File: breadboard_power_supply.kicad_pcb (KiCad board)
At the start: 2 copper layers, 50.8 x 27.8 mm, 27 parts, among them J1 Conn_02x02_Odd_Even, J2 Conn_02x02_Odd_Even, J3 Conn_02x03_Odd_Even, J4 Conn_02x03_Odd_Even, J5 7010ASV, U1 CH224K, U2 AP63205, U3 AP2205-33Y

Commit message: part placement done, started routing of top layer
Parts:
- removed C4: 10u, 0Capacitors:C_0805_2012Metric_Pad1.18x1.45mm_HandSolder
- moved R4 149.1 mm to (182.0, 78.6), turned to -90 degrees
- moved R5 145.4 mm to (178.6, 78.6), turned to -90 degrees
- moved R6 141.8 mm to (175.2, 78.6), turned to -90 degrees
- moved JP1 140.2 mm to (182.0, 74.0), turned to -90 degrees
- moved JP2 136.4 mm to (178.6, 74.0), turned to -90 degrees
- moved R3 135.5 mm to (166.6, 86.0)
- moved C8 135.0 mm to (164.2, 77.6), turned to 90 degrees
- moved U1 134.0 mm to (160.0, 86.0), turned to -90 degrees
- moved JP3 132.7 mm to (175.2, 74.0), turned to -90 degrees
- moved R1 129.5 mm to (159.2, 76.6), turned to -90 degrees
- moved C9 129.3 mm to (158.2, 82.4)
- moved C3 128.9 mm to (157.6, 76.0), turned to 90 degrees
- moved R2 127.5 mm to (159.2, 79.8), turned to -90 degrees
- moved C1 126.3 mm to (154.0, 79.2)
- moved C7 124.5 mm to (162.2, 77.6), turned to 90 degrees
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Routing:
- net /CFG2: track 0.00 -> 38.6 mm, vias 0 -> 2
- net /CFG3: track 0.00 -> 34.4 mm, vias 0 -> 2
- net /CC1: track 0.00 -> 34.2 mm, vias 0 -> 2
- net /CC2: track 0.00 -> 32.3 mm
- net /CFG1: track 0.00 -> 28.2 mm
- net /USB_P: track 0.00 -> 27.1 mm
- net /USB_N: track 0.00 -> 27.1 mm, vias 0 -> 2
- net VBUS: track 0.00 -> 19.9 mm, vias 0 -> 1
- net Net-(U1-Vdd): track 0.00 -> 4.85 mm
- net Net-(U1-VBUS): track 0.00 -> 3.18 mm
- net GND: track 0.00 -> 2.74 mm
- net Net-(U2-SW): track 0.00 -> 2.11 mm
- net Net-(R1-Pad2): track 0.00 -> 1.53 mm

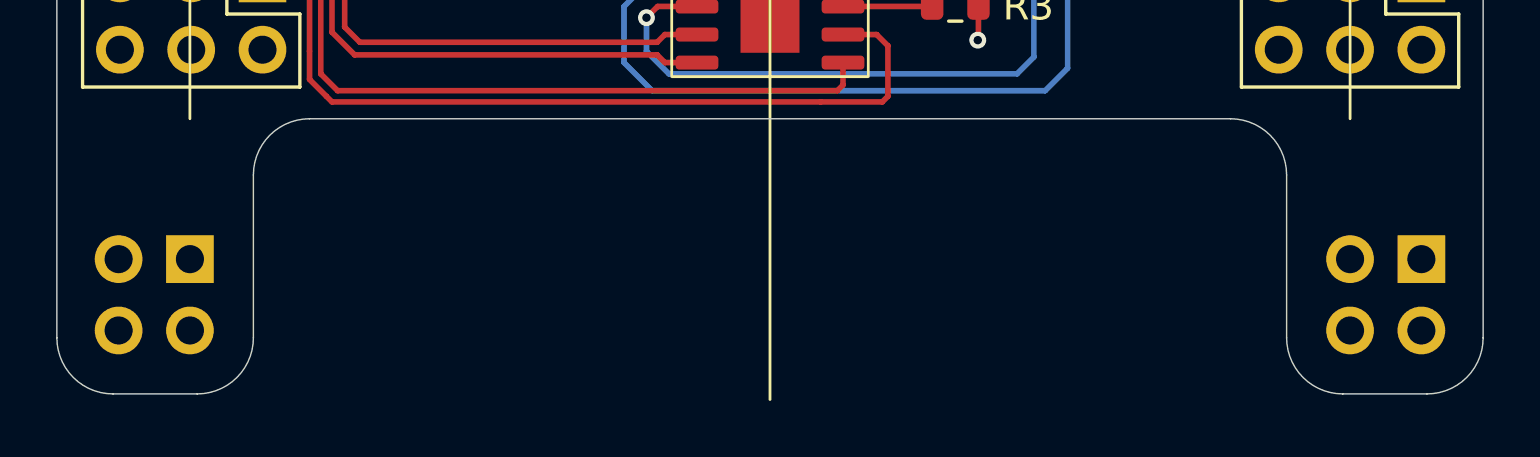
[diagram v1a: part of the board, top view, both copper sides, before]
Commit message: adjusted position for breadboard connectors
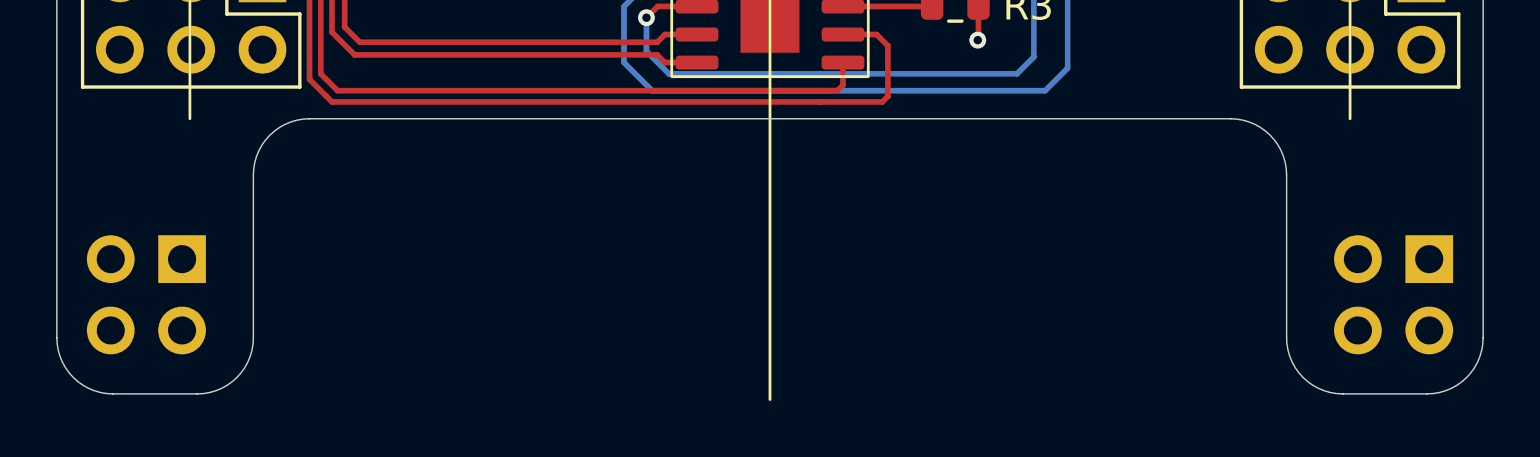
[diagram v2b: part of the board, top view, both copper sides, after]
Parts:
- moved J1 0.28 mm to (139.1, 95.0)
- moved J2 0.28 mm to (183.5, 95.0)
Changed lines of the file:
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@@
 		(tags "capacitor")
 		(property "Reference" "C1"
-			(at -2.425 0 360)
+			(at -2.425 0 0)
 			(layer "F.SilkS")
 			(effects
@@
 		)
 		(property "Value" "100n"
-			(at 0 0 360)
+			(at 0 0 0)
 			(layer "F.Fab")
 			(effects
@@
 		)
 		(fp_text user "${REFERENCE}"
-			(at 0 0 360)
+			(at 0 0 0)
 			(layer "F.Fab")
 			(effects
@@
 		(tags "capacitor handsolder")
 		(property "Reference" "C6"
-			(at -2.6 0 360)
+			(at -2.6 0 0)
 			(layer "F.SilkS")
 			(effects
@@
 		)
 		(property "Value" "10u"
-			(at 0 0 360)
+			(at 0 0 0)
 			(layer "F.Fab")
 			(effects
@@
 		)
 		(fp_text user "${REFERENCE}"
-			(at 0 0 360)
+			(at 0 0 0)
 			(layer "F.Fab")
 			(effects
@@
 		(tags "Through hole pin header THT 2x03 2.54mm double row")
 		(property "Reference" "J3"
-			(at -2.4 -0.675 -90)
+			(at -2.4 -0.675 90)
 			(layer "F.SilkS")
 			(effects
@@
 		)
 		(property "Value" "Conn_02x03_Odd_Even"
-			(at 1.27 7.41 -90)
+			(at 1.27 7.41 90)
 			(layer "F.Fab")
 			(effects
@@
 		)
 		(fp_text user "${REFERENCE}"
-			(at 1.27 2.54 180)
+			(at 1.27 2.54 360)
 			(layer "F.Fab")
 			(effects
@@
 			(pintype "passive")
 		)
-		(model "${KICAD8_3DMODEL_DIR}/Connector_PinHeader_2.54mm.3dshapes/PinHeader_2x03_P2.54mm_Vertical.wrl"
+		(model "${KICAD8_3DMODEL_DIR}/Connector_PinHeader_2.54mm.3dshapes/PinHeader_2x03_P2.54mm_Vertical.step"
 			(offset
 				(xyz 0 0 0)
@@
 			(pintype "power_out")
 		)
-		(model "${KICAD8_3DMODEL_DIR}/Package_TO_SOT_SMD.3dshapes/SOT-89-3.wrl"
+		(model "${KICAD8_3DMODEL_DIR}/Package_TO_SOT_SMD.3dshapes/SOT-89-3.step"
 			(offset
 				(xyz 0 0 0)
@@
 			(pintype "passive")
 		)
-		(model "${KICAD8_3DMODEL_DIR}/Connector_PinHeader_2.54mm.3dshapes/PinHeader_2x03_P2.54mm_Vertical.wrl"
+		(model "${KICAD8_3DMODEL_DIR}/Connector_PinHeader_2.54mm.3dshapes/PinHeader_2x03_P2.54mm_Vertical.step"
 			(offset
 				(xyz 0 0 0)
@@
 		(tags "inductor")
 		(property "Reference" "L1"
-			(at -2.7 0 360)
+			(at -2.7 0 0)
 			(layer "F.SilkS")
 			(effects
@@
 		)
 		(property "Value" "4.7uH/800mA"
-			(at 0 0 360)
+			(at 0 0 0)
 			(layer "F.Fab")
 			(effects
@@
 		)
 		(fp_text user "${REFERENCE}"
-			(at 0 0 360)
+			(at 0 0 0)
 			(layer "F.Fab")
 			(effects
@@
 		(tags "capacitor")
 		(property "Reference" "C5"
-			(at 0.6 -1.4 360)
+			(at 0.6 -1.4 0)
 			(layer "F.SilkS")
 			(effects
@@
 		)
 		(property "Value" "100n"
-			(at -0.025 0 360)
+			(at -0.025 0 0)
 			(layer "F.Fab")
 			(effects
@@
 		)
 		(fp_text user "${REFERENCE}"
-			(at 0 0 360)
+			(at 0 0 0)
 			(layer "F.Fab")
 			(effects
@@
 		)
 		(property "Value" "AP63205"
-			(at 0 2.4 360)
+			(at 0 2.4 0)
 			(layer "F.Fab")
 			(effects
@@
 		)
 		(property "Footprint" "0IC_Interfaces:SOT-23-6"
-			(at 0 0 360)
+			(at 0 0 0)
 			(layer "F.Fab")
 			(hide yes)
@@
 		)
 		(property "Datasheet" "https://www.diodes.com/assets/Datasheets/AP63200Q_AP63201Q_AP63203Q_AP63205Q.pdf"
-			(at 0 0 360)
+			(at 0 0 0)
 			(layer "F.Fab")
 			(hide yes)
@@
 		)
 		(property "Description" "Buck Switching Regulator IC Positive Fixed 5V 1 Output 2A SOT-23-6 Thin, TSOT-23-6"
-			(at 0 0 360)
+			(at 0 0 0)
 			(layer "F.Fab")
 			(hide yes)
@@
 		)
 		(fp_text user "${REFERENCE}"
-			(at 0 0 360)
+			(at 0 0 0)
 			(layer "F.Fab")
 			(effects
@@
 		(locked yes)
 		(layer "B.Cu")
-		(at 183.2 95 180)
+		(at 183.48 95 180)
 		(descr "Through hole straight pin header, 2x02, 2.54mm pitch, double rows")
 		(tags "Through hole pin header THT 2x02 2.54mm double row")
@@
 		(locked yes)
 		(layer "B.Cu")
-		(at 139.34 95 180)
+		(at 139.06 95 180)
 		(descr "Through hole straight pin header, 2x02, 2.54mm pitch, double rows")
 		(tags "Through hole pin header THT 2x02 2.54mm double row")

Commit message: added production files
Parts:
- added H1: MountingHole, MountingHole:MountingHole_2.2mm_M2_DIN965_Pad_TopBottom, F.Cu at (148.0, 82.0)
- added H2: MountingHole, MountingHole:MountingHole_2.2mm_M2_DIN965_Pad_TopBottom, F.Cu at (173.0, 87.0)
- moved C5 1.00 mm to (149.8, 76.2)
- moved C6 0.82 mm to (149.4, 74.2)
- moved L1 0.20 mm to (154.5, 73.6)
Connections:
- J3 pad 3: VCC_PD -> VBUS
- J4 pad 3: VCC_PD -> VBUS
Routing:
- net +5V: track 0.00 -> 115.2 mm, vias 0 -> 5
- net VBUS: track 19.9 -> 96.1 mm, vias 1 -> 2
- net +3.3V: track 0.00 -> 52.7 mm, vias 0 -> 5
- net GND: track 2.74 -> 14.4 mm, vias 0 -> 10
- net VCC_O2: track 0.00 -> 11.2 mm
- net VCC_O1: track 0.00 -> 10.1 mm
- net /CFG3: track 34.4 -> 38.6 mm
- net /CFG2: track 38.6 -> 42.3 mm
- added copper zone on B.Cu, net GND
- added copper zone on F.Cu, net GND
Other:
- board text added: "0"
- board text added: "1"
- board text added: "12V"
- board text added: "15V"
- board text added: "20V"
- board text added: "3v3"
- board text added: "5V"
- board text added: "5v"
- board text added: "9V"
- board text added: "GND"
- board text added: "JP1"
- board text added: "JP2"
- board text added: "JP3"
- board text added: "NC"
- board text added: "VBUS"
- board text added: "VCC"
